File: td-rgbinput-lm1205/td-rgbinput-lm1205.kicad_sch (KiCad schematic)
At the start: 10 parts, among them J2 Conn_01x07_Male, J3 Conn_01x05_Pin, J4 Conn_01x06_Male, U1 AP2205-33W5-7

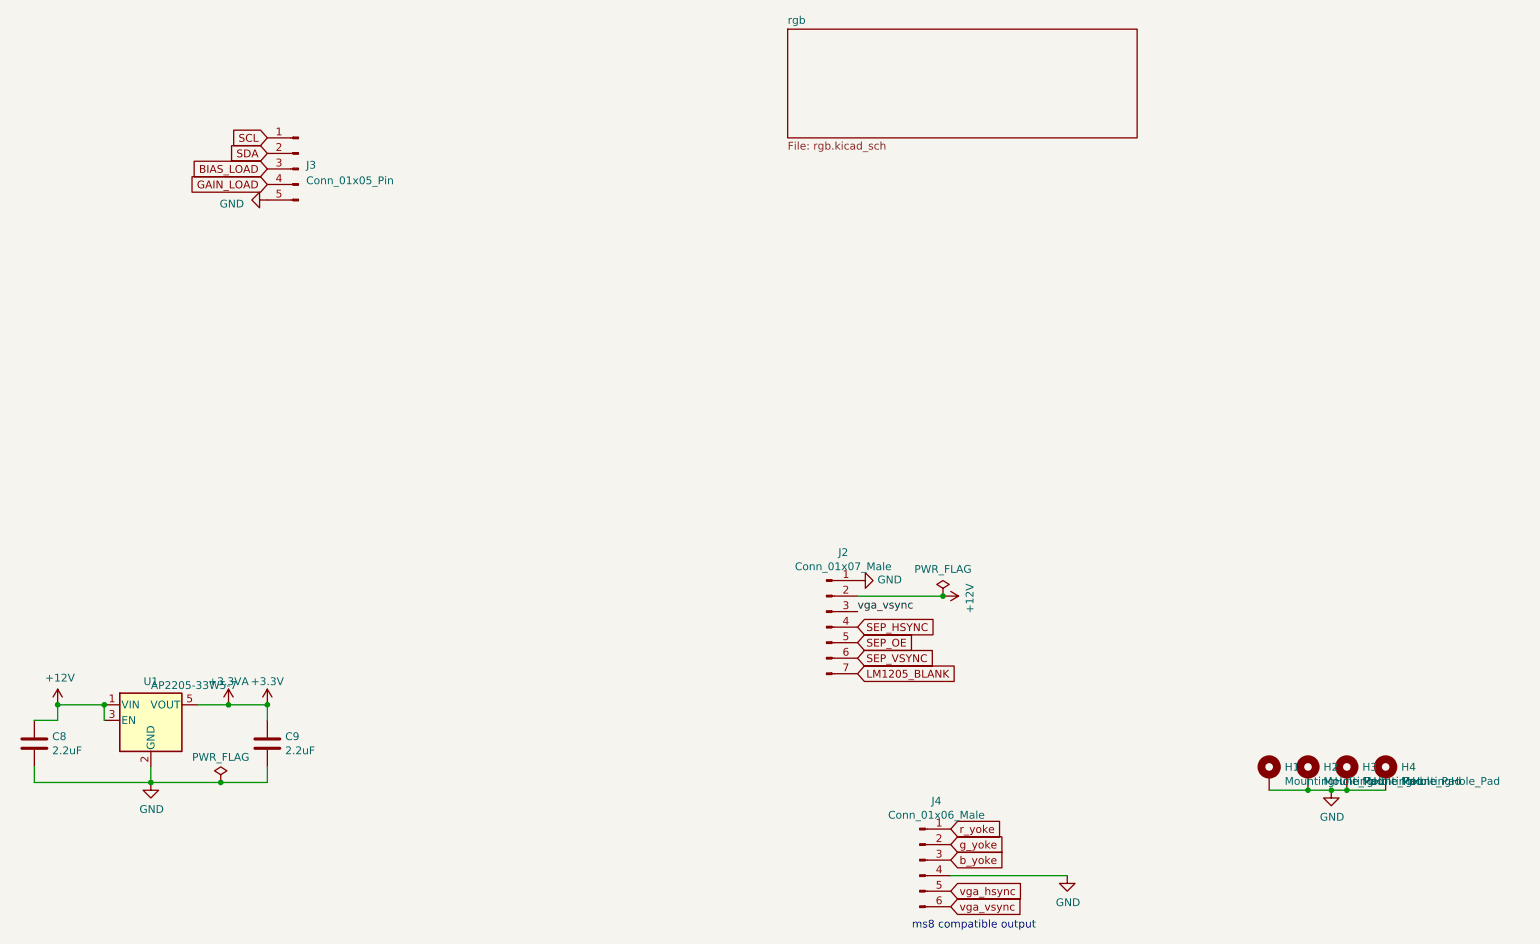
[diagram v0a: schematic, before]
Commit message: Update td-rgbinput-lm1205 to add decoupling caps etc
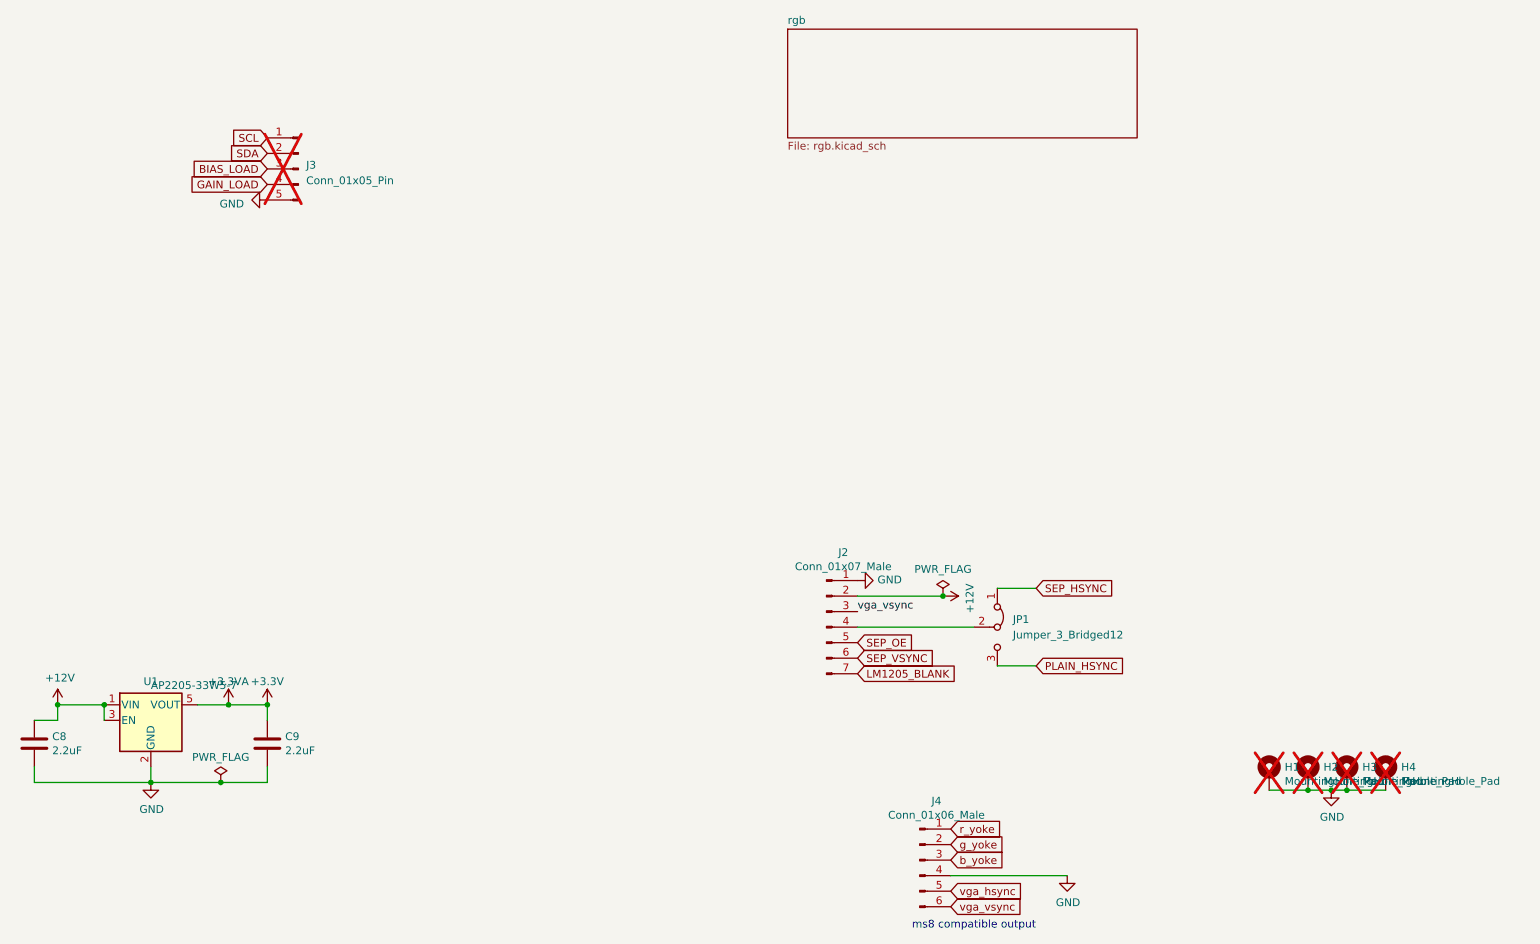
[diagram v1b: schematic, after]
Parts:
- added JP1: Jumper_3_Bridged12, Connector_PinHeader_2.54mm:PinHeader_1x03_P2.54mm_Vertical, symbol Jumper:Jumper_3_Bridged12
- H1, H2, H3, H4, J3: now not fitted
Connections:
- net SEP_HSYNC: now also JP1.1 (A); no longer J2.4 (Pin_4)
- new net: J2.4 (Pin_4), JP1.2 (C)
- new net PLAIN_HSYNC: JP1.3 (B)
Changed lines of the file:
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@@
 (kicad_sch
-	(version 20231120)
+	(version 20250114)
 	(generator "eeschema")
-	(generator_version "8.0")
+	(generator_version "9.0")
 	(paper "A3")
+	(text "ms8 compatible output"
+		(exclude_from_sim no)
+		(at 254 252.73 0)
+		(effects
+			(font
+				(size 1.27 1.27)
+			)
+			(justify left bottom)
+		)
+	)
 	(junction
 		(at 129.54 228.6)
@@
 	(wire
 		(pts
+			(xy 245.11 203.2) (xy 264.16 203.2)
+		)
+		(stroke
+			(width 0)
+			(type default)
+		)
+	)
+	(wire
+		(pts
+			(xy 267.97 209.55) (xy 274.32 209.55)
+		)
+		(stroke
+			(width 0)
+			(type default)
+		)
+	)
+	(wire
+		(pts
 			(xy 110.49 228.6) (xy 129.54 228.6)
 		)
@@
 		)
 	)
-	(text "ms8 compatible output"
-		(exclude_from_sim no)
-		(at 254 252.73 0)
-		(effects
-			(font
-				(size 1.27 1.27)
-			)
-			(justify left bottom)
+	(wire
+		(pts
+			(xy 267.97 196.85) (xy 274.32 196.85)
+		)
+		(stroke
+			(width 0)
+			(type default)
 		)
 	)
 	(label "vga_vsync"
 		(at 245.11 200.66 0)
-		(fields_autoplaced yes)
 		(effects
 			(font
@@
 	(global_label "SEP_HSYNC"
 		(shape input)
-		(at 245.11 203.2 0)
+		(at 274.32 196.85 0)
 		(fields_autoplaced yes)
 		(effects
@@
 		)
 		(property "Intersheetrefs" "${INTERSHEET_REFS}"
-			(at 258.1868 203.2 0)
+			(at 287.3968 196.85 0)
 			(effects
 				(font
@@
 		)
 	)
+	(global_label "PLAIN_HSYNC"
+		(shape input)
+		(at 274.32 209.55 0)
+		(fields_autoplaced yes)
+		(effects
+			(font
+				(size 1.27 1.27)
+			)
+			(justify left)
+		)
+		(property "Intersheetrefs" "${INTERSHEET_REFS}"
+			(at 289.1697 209.55 0)
+			(effects
+				(font
+					(size 1.27 1.27)
+				)
+				(justify left)
+				(hide yes)
+			)
+		)
+	)
 	(global_label "LM1205_BLANK"
 		(shape input)
@@
 		(in_bom yes)
 		(on_board yes)
-		(dnp no)
+		(dnp yes)
 		(property "Reference" "H1"
 			(at 314.96 226.0854 0)
@@
 		(in_bom yes)
 		(on_board yes)
-		(dnp no)
+		(dnp yes)
 		(property "Reference" "H2"
 			(at 321.31 226.0854 0)
@@
 		(in_bom yes)
 		(on_board yes)
-		(dnp no)
+		(dnp yes)
 		(property "Reference" "H3"
 			(at 327.66 226.0854 0)
@@
 		(in_bom yes)
 		(on_board yes)
-		(dnp no)
+		(dnp yes)
 		(property "Reference" "H4"
 			(at 334.01 226.0854 0)
@@
 		(in_bom yes)
 		(on_board yes)
-		(dnp no)
+		(dnp yes)
 		(fields_autoplaced yes)
 		(property "Reference" "J3"
@@
 				(path "/3efa2ece-8f3f-4a8c-96e9-6ab3ec6f1f70"
 					(reference "J3")
+					(unit 1)
+				)
+			)
+		)
+	)
+	(symbol
+		(lib_id "Jumper:Jumper_3_Bridged12")
+		(at 267.97 203.2 270)
+		(unit 1)
+		(exclude_from_sim no)
+		(in_bom no)
+		(on_board yes)
+		(dnp no)
+		(fields_autoplaced yes)
+		(property "Reference" "JP1"
+			(at 270.51 201.9299 90)
+			(effects
+				(font
+					(size 1.27 1.27)
+				)
+				(justify left)
+			)
+		)
+		(property "Value" "Jumper_3_Bridged12"
+			(at 270.51 204.4699 90)
+			(effects
+				(font
+					(size 1.27 1.27)
+				)
+				(justify left)
+			)
+		)
+		(property "Footprint" "Connector_PinHeader_2.54mm:PinHeader_1x03_P2.54mm_Vertical"
+			(at 267.97 203.2 0)
+			(effects
+				(font
+					(size 1.27 1.27)
+				)
+				(hide yes)
+			)
+		)
+		(property "Datasheet" "~"
+			(at 267.97 203.2 0)
+			(effects
+				(font
+					(size 1.27 1.27)
+				)
+				(hide yes)
+			)
+		)
+		(property "Description" "Jumper, 3-pole, pins 1+2 closed/bridged"
+			(at 267.97 203.2 0)
+			(effects
+				(font
+					(size 1.27 1.27)
+				)
+				(hide yes)
+			)
+		)
+		(pin "1"
+		)
+		(pin "3"
+		)
+		(pin "2"
+		)
+		(instances
+			(project ""
+				(path "/3efa2ece-8f3f-4a8c-96e9-6ab3ec6f1f70"
+					(reference "JP1")
 					(unit 1)
 				)
@@
 		(at 233.68 105.41)
 		(size 57.15 17.78)
+		(exclude_from_sim no)
+		(in_bom yes)
+		(on_board yes)
+		(dnp no)
 		(fields_autoplaced yes)
 		(stroke
@@
 		)
 	)
+	(embedded_fonts no)
 )

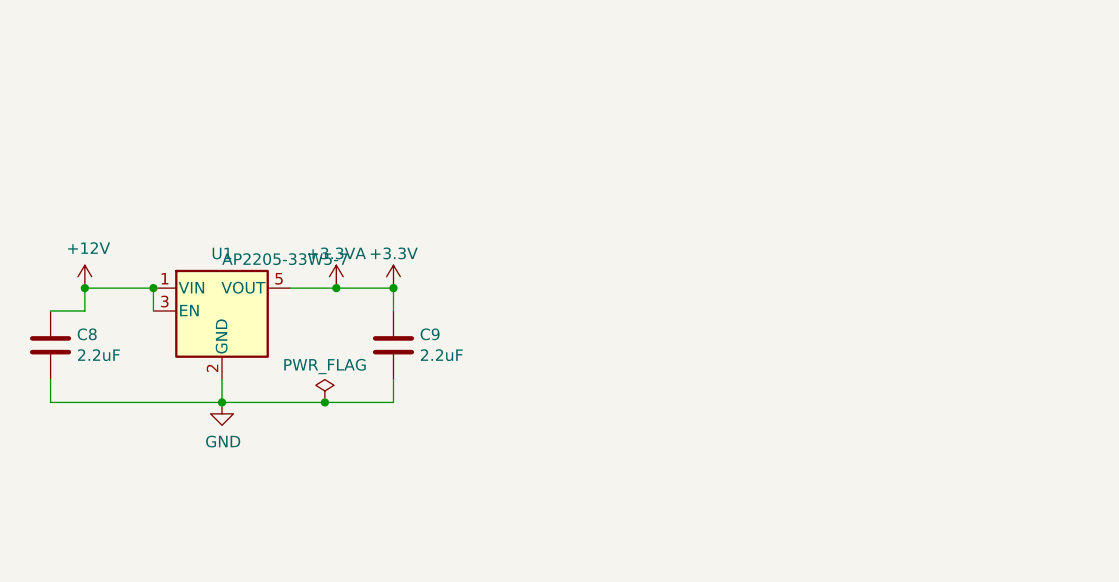
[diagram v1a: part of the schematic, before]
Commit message: Update td-rgbinput-lm1205 to add a linear regulator.
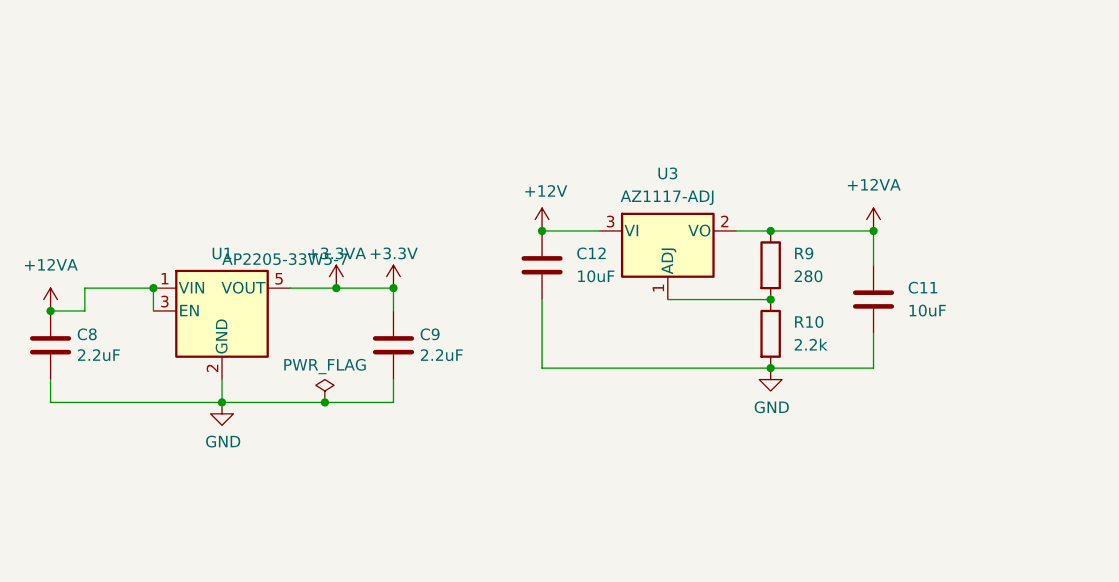
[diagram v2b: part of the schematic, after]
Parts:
- added C11, C12: 10uF, Capacitor_SMD:C_0805_2012Metric, symbol Device:C
- added R10: 2.2k, Resistor_SMD:R_0805_2012Metric, symbol Device:R
- added R9: 280, Resistor_SMD:R_0805_2012Metric, symbol Device:R
- added U3: AZ1117-ADJ, Package_TO_SOT_SMD:SOT-223-3_TabPin2, symbol Regulator_Linear:AZ1117-ADJ
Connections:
- net +12V: now also C12.1, U3.3 (VI); no longer C8.1, U1.1 (VIN), U1.3 (EN)
- net GND: now also C11.2, C12.2, R10.2
- new net: R10.1, R9.2, U3.1 (ADJ)
- new net +12VA: C11.1, C8.1, R9.1, U1.1 (VIN), U1.3 (EN), U3.2 (VO)

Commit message: bunch of random updates
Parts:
- C11, C12: Digikey (none) -> 490-10516-1-ND
- R10: Digikey 311-2.2KCRCT-ND -> 311-2.20KCRCT-ND
- U3: Digikey (none) -> AZ1117CH-ADJTRG1DICT-ND
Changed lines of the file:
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@@
+			)
+		)
+		(property "Digikey" "490-10516-1-ND"
+			(at 165.1 213.36 0)
+			(effects
+				(font
+					(size 1.27 1.27)
+				)
+				(hide yes)
 			)
 		)
@@
 			)
 		)
+		(property "Digikey" "AZ1117CH-ADJTRG1DICT-ND"
+			(at 179.07 209.55 0)
+			(effects
+				(font
+					(size 1.27 1.27)
+				)
+				(hide yes)
+			)
+		)
 		(pin "2"
 		)
@@
 			)
 		)
-		(property "Digikey" "311-2.2KCRCT-ND"
+		(property "Digikey" "311-2.20KCRCT-ND"
 			(at 190.5 220.98 0)
 			(effects
@@
 			(at 201.93 217.17 0)
 			(effects
+				(font
+					(size 1.27 1.27)
+				)
+				(hide yes)
+			)
+		)
+		(property "Digikey" "490-10516-1-ND"
+			(at 201.93 217.17 0)
+			(effects
